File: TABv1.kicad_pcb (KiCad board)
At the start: 4 copper layers, 85 x 45 mm, 127 parts, among them IC1 TPS630702RNMR, J1 USB_C_Receptacle_USB2.0_16P, J10 Conn_UART_HOST, J11 Conn_UART_1, J12 Conn_UART_0, J13 Conn_ADC, J14 Conn_BATT, J15 DB141R-2.54-8P-GN, J2 Conn_02x03_Row_Letter_Last, J3 Conn_02x03_Row_Letter_Last, J6 SWD, J7 503398-1892, J8 Conn_SPI1, J9 Conn_SPI0, Q1 MJD44H11T4G, Q10 PJM09P30DF, Q11 PJM09P30DF, Q12 PJM09P30DF, Q13 PJM09P30DF, Q2 NMOS, Q5 NMOS, Q6 NMOS, Q7 NMOS, Q8 NMOS, Q9 NMOS, SW1 BOOTSEL, SW2 RESET, SW3 RESET, SW4 RESET, U1 RP2350B-QFN80, U2 W25Q128JVS, U3 BMP390, U4 LSM6DSO32TR, U6 LT3092xST, U7 LSM6DSO32TR, U8 LIS2MDL, Y1 12MHz

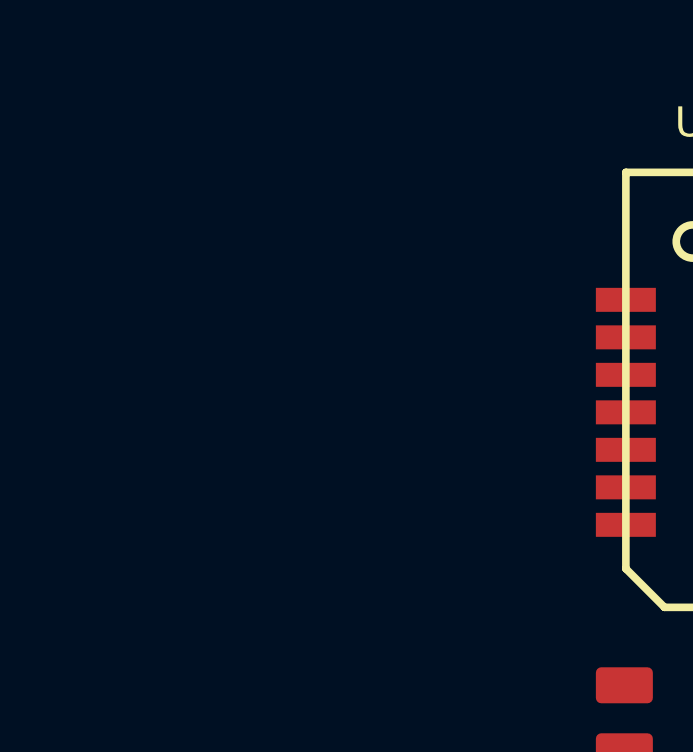
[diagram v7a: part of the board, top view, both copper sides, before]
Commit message: Lora radio and gps small additions
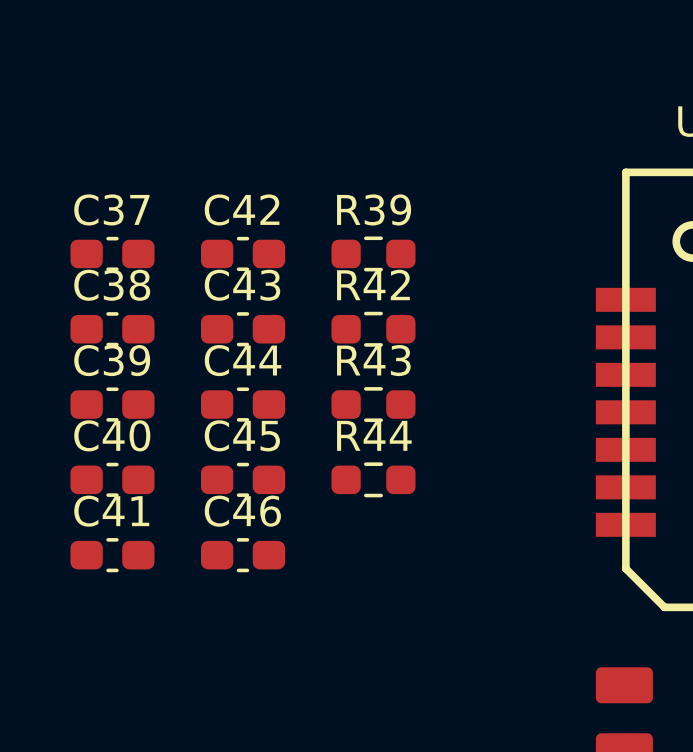
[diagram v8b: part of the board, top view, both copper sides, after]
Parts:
- added C37: 10uF, Capacitor_SMD:C_0603_1608Metric_Pad1.08x0.95mm_HandSolder, F.Cu at (47.9, 91.5)
- added C38: 100nF, Capacitor_SMD:C_0603_1608Metric_Pad1.08x0.95mm_HandSolder, F.Cu at (47.9, 94.0)
- added C39: 33pF, Capacitor_SMD:C_0603_1608Metric_Pad1.08x0.95mm_HandSolder, F.Cu at (47.9, 96.5)
- added C40: 10uF, Capacitor_SMD:C_0603_1608Metric_Pad1.08x0.95mm_HandSolder, F.Cu at (47.9, 99.0)
- added C41: 100nF, Capacitor_SMD:C_0603_1608Metric_Pad1.08x0.95mm_HandSolder, F.Cu at (47.9, 101.5)
- added C42: 33pF, Capacitor_SMD:C_0603_1608Metric_Pad1.08x0.95mm_HandSolder, F.Cu at (52.2, 91.5)
- added C43: 4.7uF, Capacitor_SMD:C_0603_1608Metric_Pad1.08x0.95mm_HandSolder, F.Cu at (52.2, 94.0)
- added C44: 0.1uF, Capacitor_SMD:C_0603_1608Metric_Pad1.08x0.95mm_HandSolder, F.Cu at (52.2, 96.5)
- added C45: 100n, Capacitor_SMD:C_0603_1608Metric_Pad1.08x0.95mm_HandSolder, F.Cu at (52.2, 99.0)
- added C46: 100n, Capacitor_SMD:C_0603_1608Metric_Pad1.08x0.95mm_HandSolder, F.Cu at (52.2, 101.5)
- added R39: R_Small, Resistor_SMD:R_0603_1608Metric_Pad0.98x0.95mm_HandSolder, F.Cu at (56.6, 91.5)
- added R42: 220, Resistor_SMD:R_0603_1608Metric_Pad0.98x0.95mm_HandSolder, F.Cu at (56.6, 94.0)
- added R43: 220, Resistor_SMD:R_0603_1608Metric_Pad0.98x0.95mm_HandSolder, F.Cu at (56.6, 96.5)
- added R44: 10K, Resistor_SMD:R_0603_1608Metric_Pad0.98x0.95mm_HandSolder, F.Cu at (56.6, 99.0)
- SW4: value RESET -> BOOT
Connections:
- SW3 pad 1: Net-(U10-RST) -> -BATT
- SW3 pad 2: -BATT -> Net-(U10-RST)
- SW4 pad 1: Net-(U10-PH3) -> +3.3V
- SW4 pad 2: +3.3V -> Net-(U10-PH3)
- U10 pad 15: unconnected-(U10-GND-Pad15) -> -BATT
